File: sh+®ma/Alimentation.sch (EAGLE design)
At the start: 17 parts, among them X1 87758-4016

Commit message: Carte mère (résolution problème transfo)
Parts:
- removed H1, H2: MOUNT-PAD-SQUARE3.0, holes:MOUNT-PAD-SQUARE3.0
- removed TR1: (no value), trafo:EI54-1B
- added PAD1, PAD10, PAD2, PAD7, PAD8, PAD9: (no value), wirepad:2,54/1,1
- added SV1: (no value), con-lstb:MA20-2
- added X3, X4, X5, X6, X7, X8: (no value), con-molex:KK-156-4
- C2, C4: device rcl:C-EU050-075X075 -> capacitor-wima:C22/6
- X1: value 87758-4016 -> TSW-101-02-S-Q; device con-molex:87758-4016 -> con-samtec:TSW-101-02-S-Q
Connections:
- removed net N$8 (its old number): C4.2, D1.A, D2.C, LM338K.OUT, R1.2, X1-2.S
- new net N$10: C4.2, D1.A, D2.C, LM338K.OUT, R1.2, SV1.39, X3-1.S, X4-1.S, X5-1.S, X6-1.S, X7-1.S, X8-1.S
- new net N$7: SV1.38, X3-3.S, X4-3.S, X5-3.S, X6-3.S, X7-3.S, X8-3.S
- new net N$9: SV1.40, X3-2.S, X4-2.S, X5-2.S, X6-2.S, X7-2.S, X8-2.S
- net N$1: now also PAD9.P, X1-2.1; no longer PAD4.P, TR1.S4
- net N$2: now also PAD10.P, X1-1.1; no longer PAD5.P, TR1.S3
- net N$3: now also SV1.35, X3-4.S, X4-4.S, X5-4.S, X6-4.S, X7-4.S, X8-4.S; no longer X1-6.S
- net N$5: now also PAD2.P, PAD4.P, PAD8.P; no longer H1.MOUNT, TR1.P1
- net N$6: now also PAD1.P, PAD5.P, PAD7.P; no longer H2.MOUNT, TR1.P2
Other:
- moved on the sheet: X1-1, X1-2

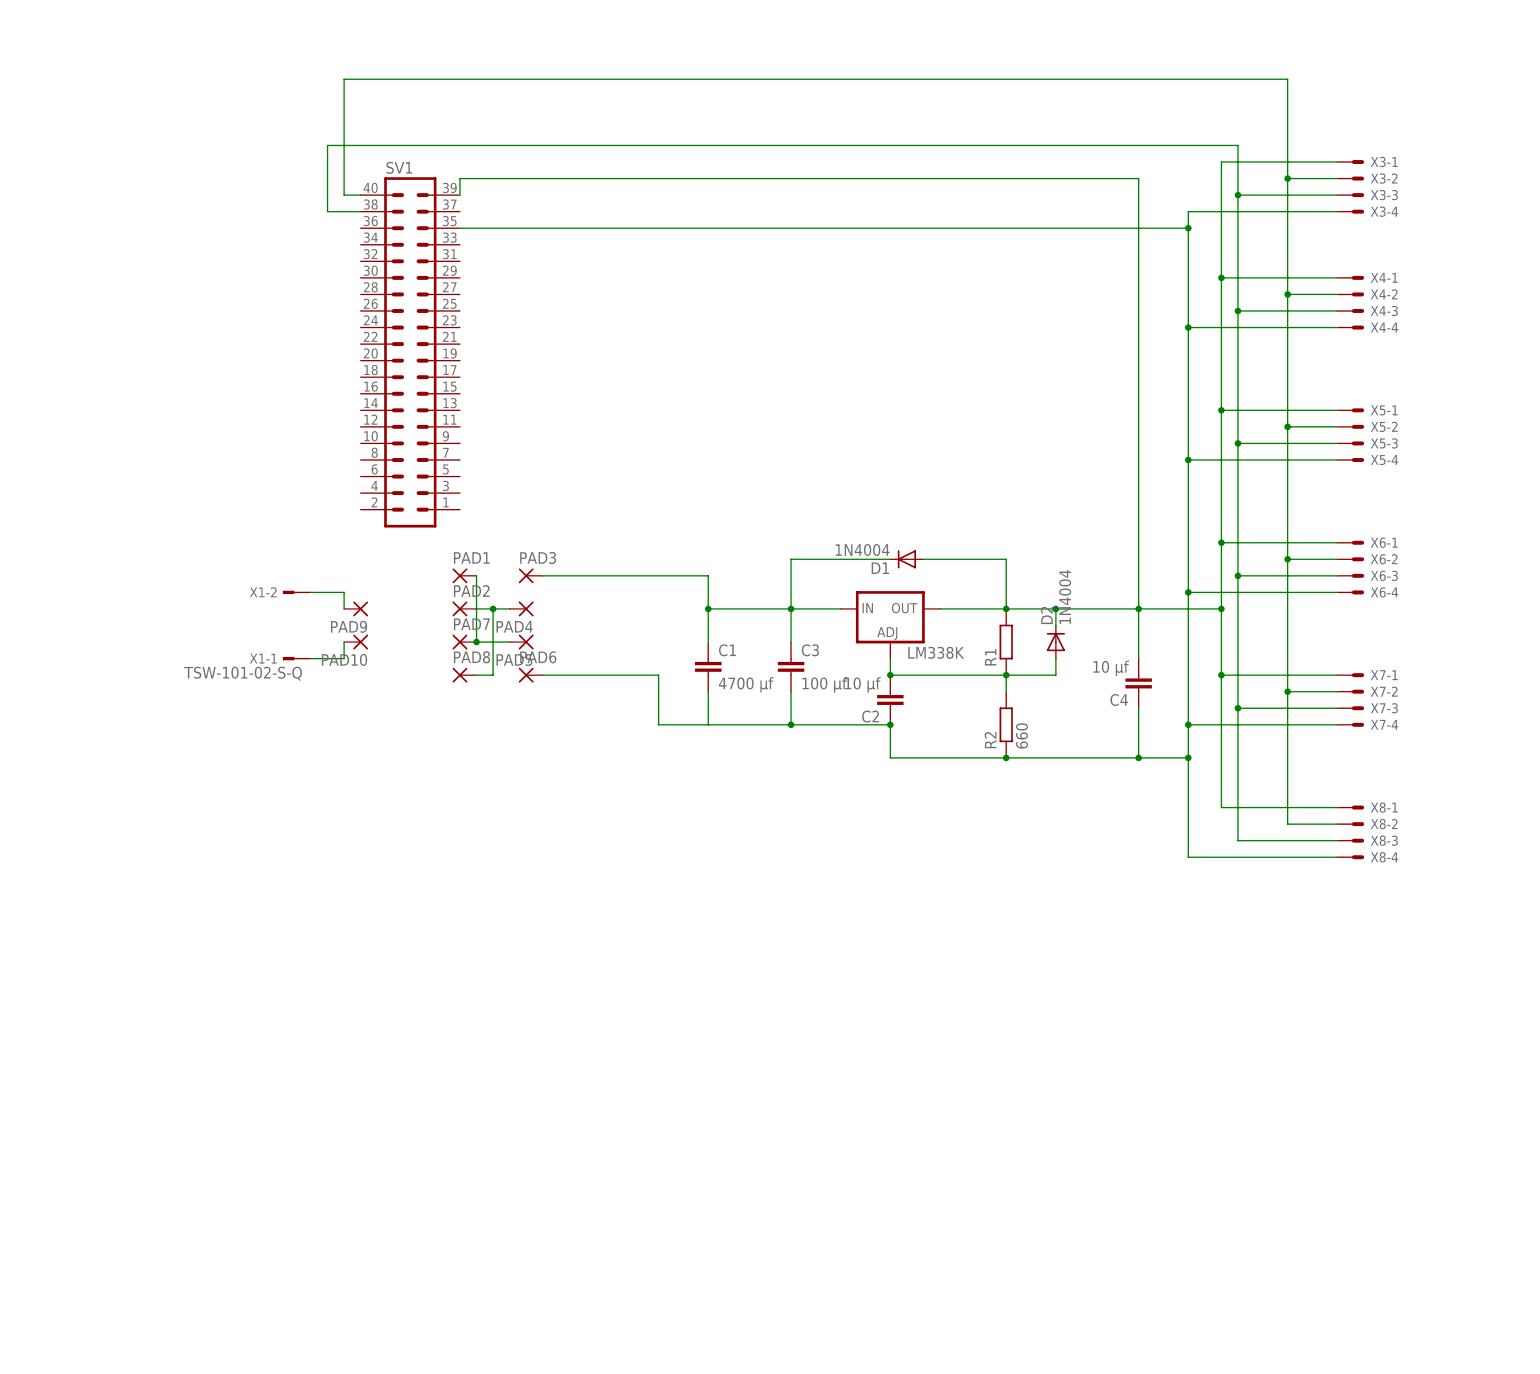
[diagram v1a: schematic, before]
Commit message: Plan du soutien de l'écran + carte mère + écran
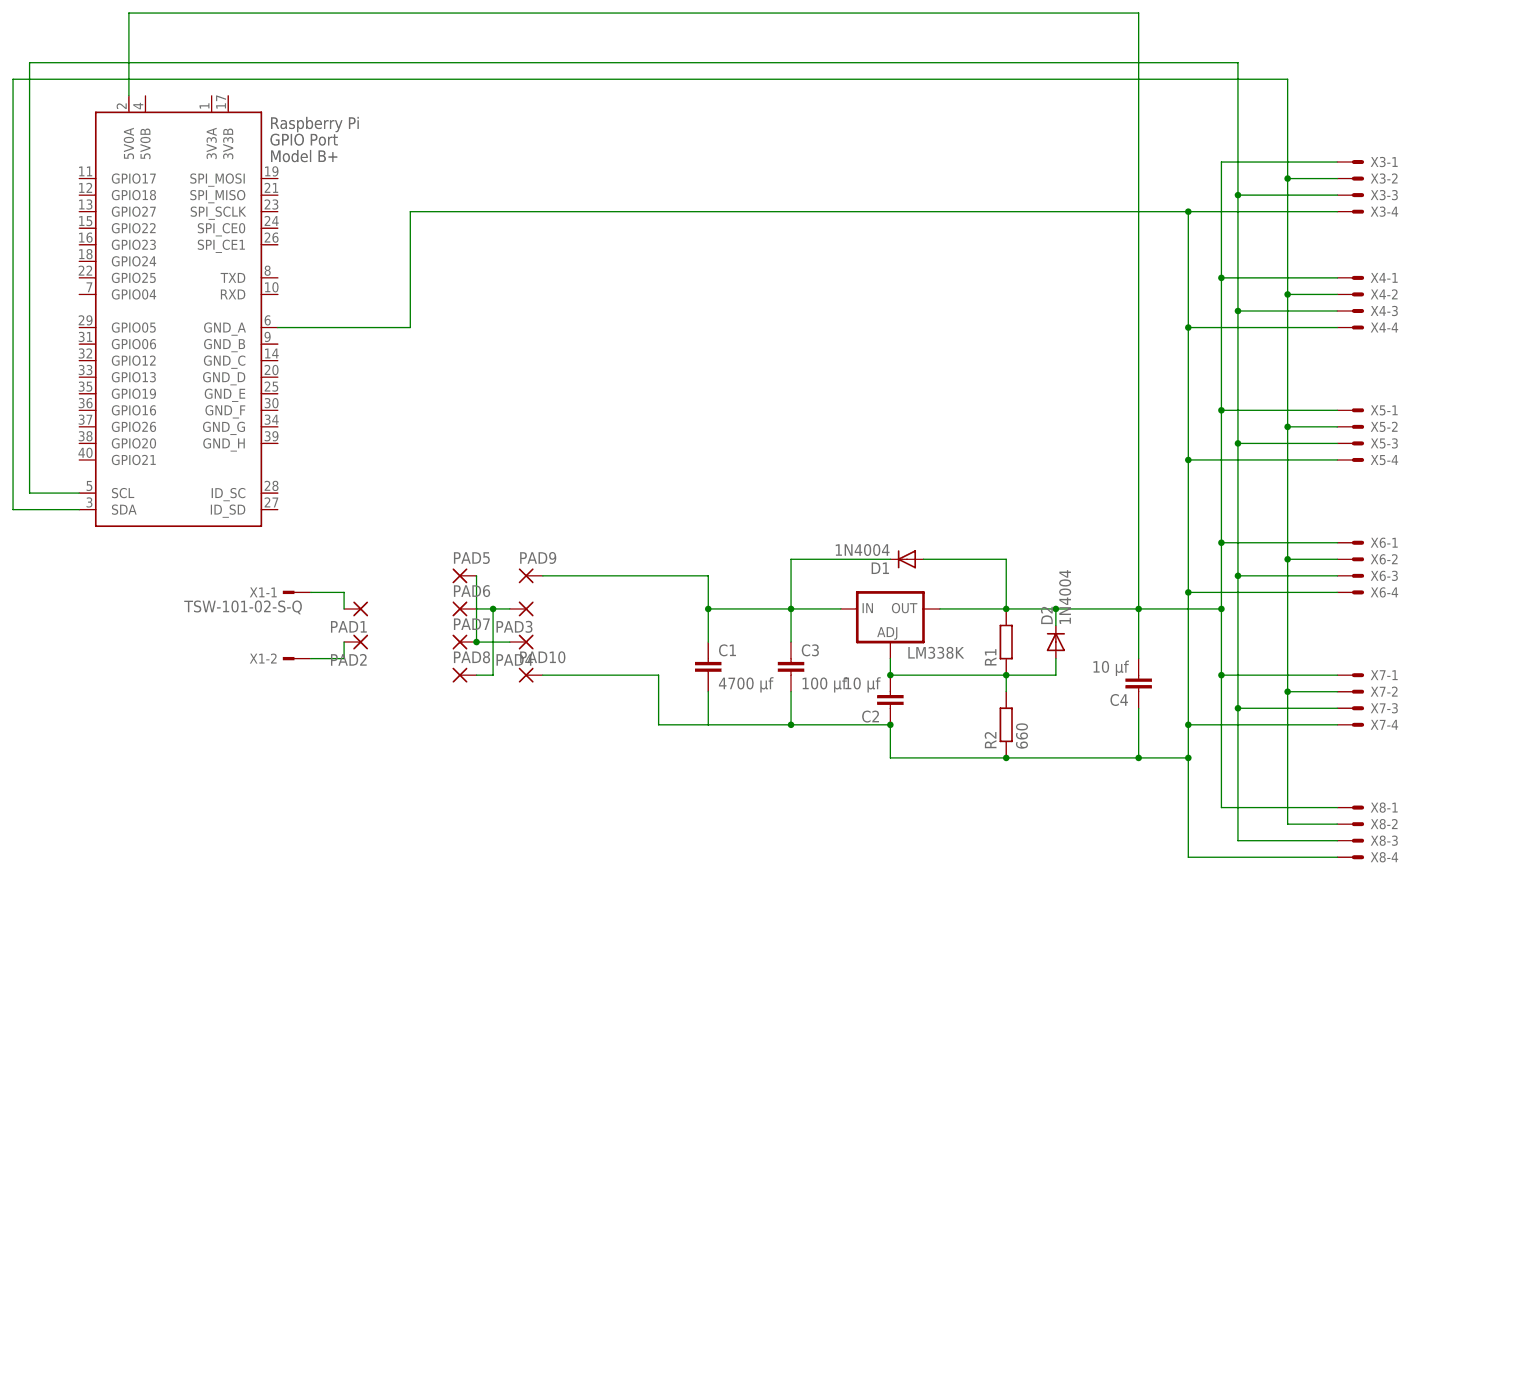
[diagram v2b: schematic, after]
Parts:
- removed SV1: (no value), con-lstb:MA20-2
- added X2: RASPI_GPIO_B+#_PIN, raspberrypi_Bastelstube_v13:RASPI_GPIO_B+#_PIN
- PAD1, PAD10, PAD2, PAD3, PAD4, PAD5, PAD6, PAD7, PAD8, PAD9: device wirepad:2,54/1,1 -> wirepad:1,6/0,8
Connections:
- net N$1: now also PAD1.P, X1-1.1; no longer PAD9.P, X1-2.1
- net N$10: now also X2.5V0A; no longer SV1.39
- net N$2: now also PAD2.P, X1-2.1; no longer PAD10.P, X1-1.1
- net N$3: now also PAD10.P, X2.GND_A; no longer PAD6.P, SV1.35
- net N$4: now also PAD9.P; no longer PAD3.P
- net N$5: now also PAD3.P, PAD6.P; no longer PAD2.P, PAD4.P
- net N$6: now also PAD4.P; no longer PAD1.P
- net N$7: now also X2.SCL; no longer SV1.38
- net N$9: now also X2.SDA; no longer SV1.40
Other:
- moved on the sheet: X1-1, X1-2

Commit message: typon + plaque fond
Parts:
- removed X4, X6, X7, X8: (no value), con-molex:KK-156-4
- added R3, R4: 220, rcl:R-EU_0309/12
- added SV1: (no value), con-lsta:FE08-1
- added X10, X11, X12, X13, X14, X9: MKS1854-6-0-404, con-stocko:MKS1854-6-0-404
- PAD1, PAD10, PAD2, PAD3, PAD4, PAD5, PAD6, PAD7, PAD8, PAD9: value (none) -> WIREPAD3,17/1,3; device wirepad:1,6/0,8 -> wirepad:WIREPAD3,17/1,3
- R2: value 660 -> 220
- X3: value (none) -> MKS1854-6-0-404; device con-molex:KK-156-4 -> con-stocko:MKS1854-6-0-404
- X5: value (none) -> MKS1852-6-0-202; device con-molex:KK-156-4 -> con-stocko:MKS1852-6-0-202
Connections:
- new net N$11: R3.2, R4.1
- new net N$12: SV1.5, X10.2, X11.2, X12.2, X13.2, X14.2, X2.SCL, X3.2, X9.2
- net N$10: now also SV1.1, X10.4, X11.4, X12.4, X13.4, X14.4, X3.4, X5.2, X9.4; no longer X3-1.S, X4-1.S, X5-1.S, X6-1.S, X7-1.S, X8-1.S
- net N$3: now also SV1.2, X10.1, X11.1, X12.1, X13.1, X14.1, X3.1, X5.1, X9.1; no longer X3-4.S, X4-4.S, X5-4.S, X6-4.S, X7-4.S, X8-4.S
- net N$7: now also SV1.6, X10.3, X11.3, X12.3, X13.3, X14.3, X2.SDA, X3.3, X9.3; no longer X2.SCL, X3-3.S, X4-3.S, X5-3.S, X6-3.S, X7-3.S, X8-3.S
- net N$8: now also R4.2; no longer R2.2
- net N$9: now also R2.2, R3.1; no longer X2.SDA, X3-2.S, X4-2.S, X5-2.S, X6-2.S, X7-2.S, X8-2.S
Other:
- moved on the sheet: R2
